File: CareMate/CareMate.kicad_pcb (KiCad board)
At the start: 2 copper layers, 19 parts, among them J1 Barrel_Jack_MountingPin, J2 Conn_01x16, J3 Conn_01x03, J4 Conn_01x03, J5 Conn_01x06, J6 Conn_01x03, J7 Conn_01x03, J8 Conn_01x02, U1 L7805, U2 LM386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

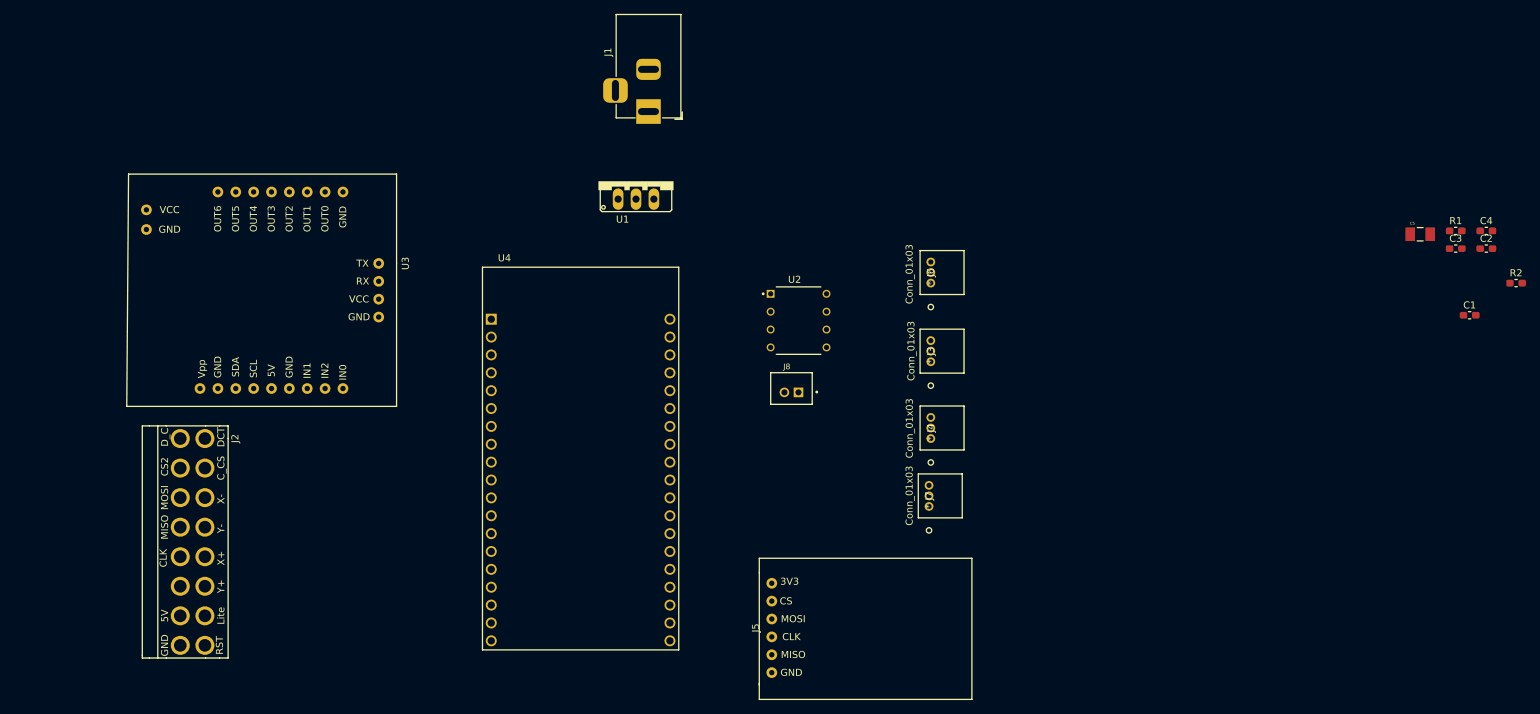
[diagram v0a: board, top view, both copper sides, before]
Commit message: significant PCB modifications including changes to elechouse footprint
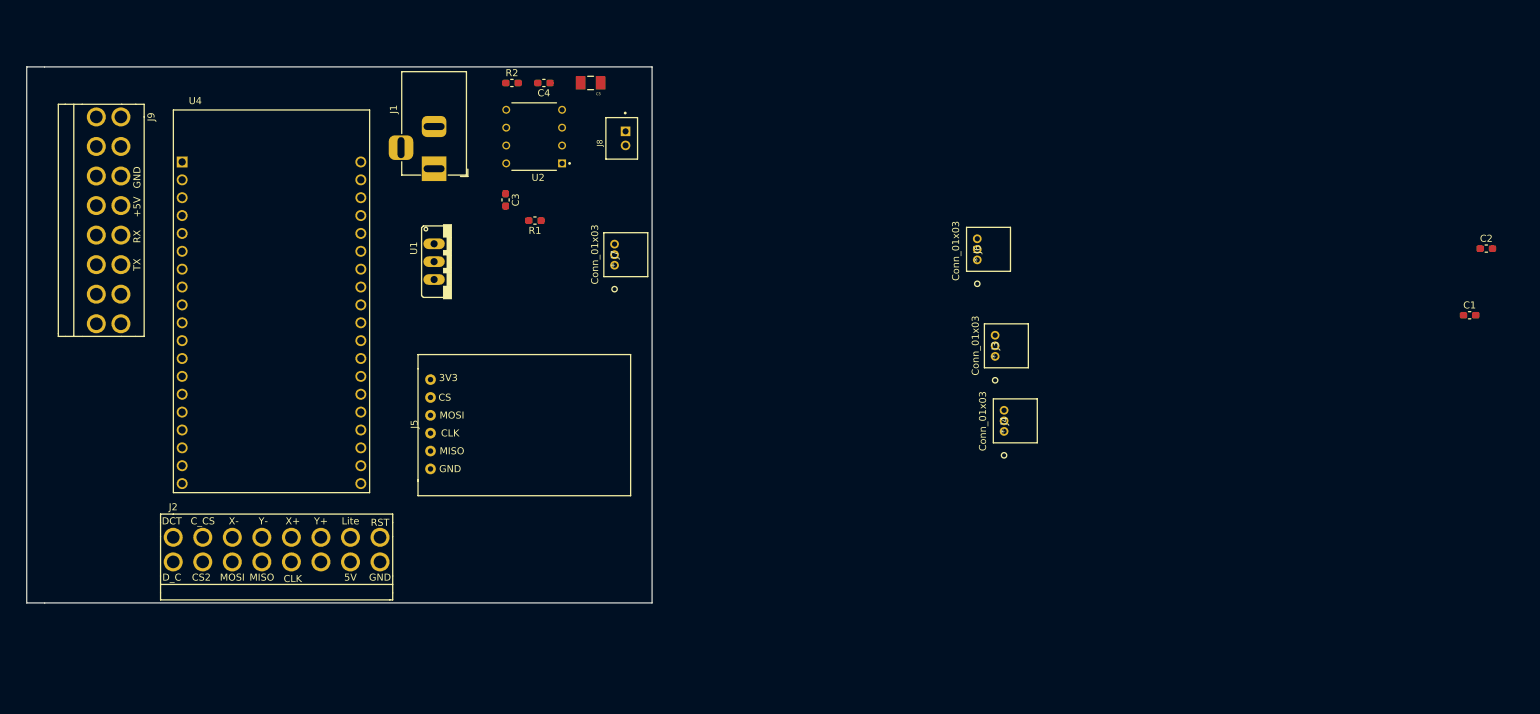
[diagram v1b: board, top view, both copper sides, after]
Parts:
- removed U3: Elechouse_V3, Additional Libraries:ElechouseV3
- added J9: ElechouseV3, Additional Libraries:16PinConnector, F.Cu at (63.8, 32.5)
- J2: value Conn_01x16 -> Touchscreen
- moved R2 145.6 mm to (117.2, 27.7)
- moved C4 135.6 mm to (121.8, 27.7), turned to 180 degrees
- moved C3 135.2 mm to (116.3, 44.3), turned to 270 degrees
- moved R1 130.9 mm to (120.5, 47.2), turned to 180 degrees
- moved C5 119.9 mm to (128.4, 27.7), turned to 180 degrees
- moved J5 56.5 mm to (105.7, 76.2)
- moved J7 56.3 mm to (131.8, 53.6)
- moved U4 49.3 mm to (83.1, 58.7)
- moved U2 45.8 mm to (120.4, 35.3), turned to 180 degrees
- moved J8 43.0 mm to (132.8, 35.6), turned to 90 degrees
- moved J1 31.5 mm to (106.2, 39.9)
- moved U1 28.5 mm to (108.7, 53.1), turned to 270 degrees
- moved J2 13.6 mm to (69.1, 90.2), turned to 0 degrees
- moved J4 10.5 mm to (187.2, 77.2)
- moved J3 9.18 mm to (185.9, 66.5)
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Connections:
- U1 pad 1: (no net) -> +9V
- U1 pad 2: (no net) -> GND
- U1 pad 3: (no net) -> +5V
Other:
- board outline added: 88.9 x 76.2 mm

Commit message: began running traces
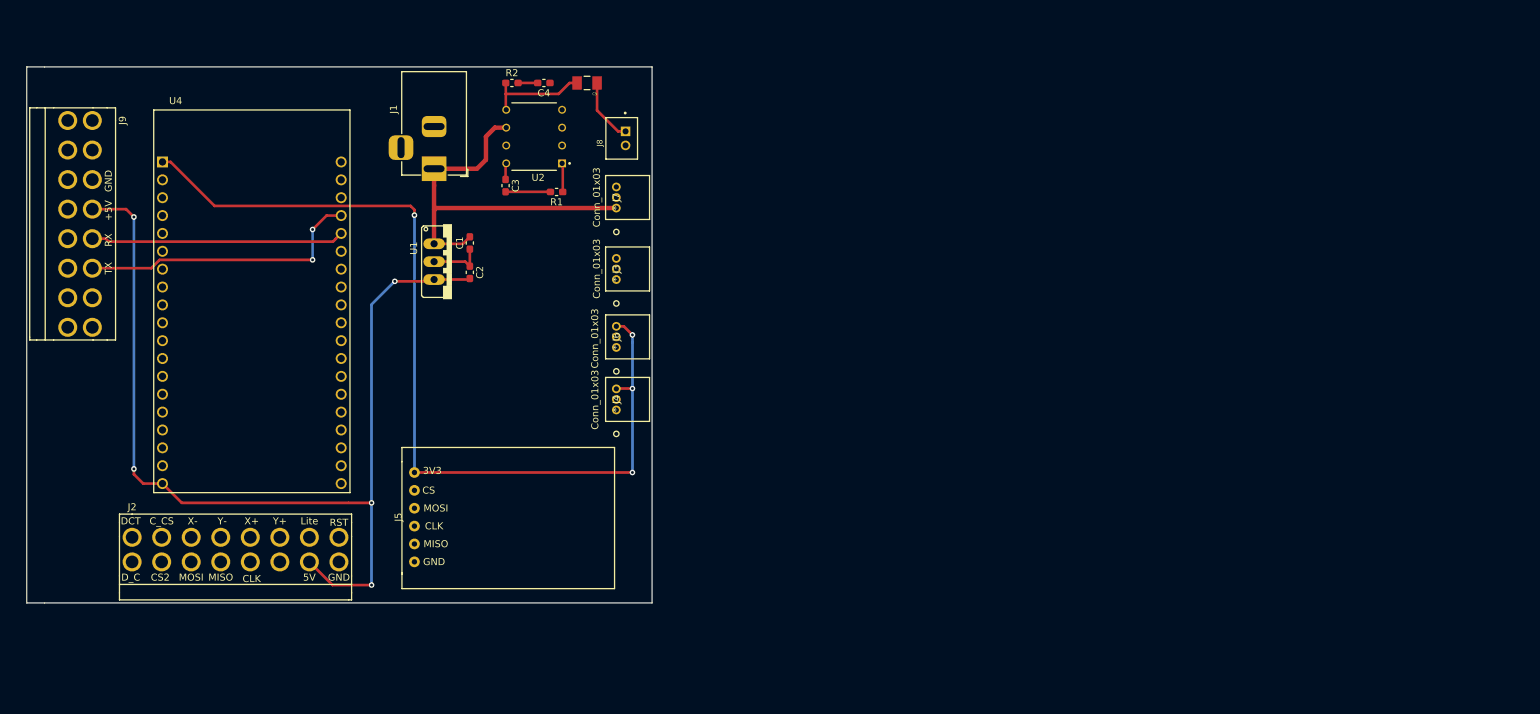
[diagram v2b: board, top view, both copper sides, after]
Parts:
- moved C2 144.5 mm to (111.3, 54.6), turned to 270 degrees
- moved C1 142.5 mm to (111.3, 50.4), turned to 90 degrees
- moved J4 55.2 mm to (132.1, 74.2)
- moved J3 54.9 mm to (132.1, 55.6)
- moved J6 52.8 mm to (132.1, 65.3)
- moved J5 13.4 mm to (103.4, 89.4)
- moved J7 8.13 mm to (132.1, 45.5)
- moved J2 5.84 mm to (63.2, 90.2)
- moved R1 5.10 mm to (123.6, 43.2)
- moved J9 4.10 mm to (59.7, 33.0)
- moved U4 2.79 mm to (80.3, 58.7)
- moved C3 2.03 mm to (116.3, 42.3)
- moved C5 0.51 mm to (127.9, 27.7)
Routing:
- net +5V: track 0.00 -> 144.0 mm, vias 0 -> 5
- net 3.3V: track 0.00 -> 131.6 mm, vias 0 -> 4
- net +9V: track 0.00 -> 56.8 mm
- net Tx_VoiceRec: track 0.00 -> 41.0 mm, vias 0 -> 2
- net Rx_VoiceRec: track 0.00 -> 36.0 mm
- net Net-(C5-Pad2): track 0.00 -> 14.6 mm
- net Amp_Output: track 0.00 -> 9.18 mm
- net GND: track 0.00 -> 7.78 mm
- net Net-(C3-Pad2): track 0.00 -> 6.39 mm
- net Net-(R1-Pad1): track 0.00 -> 4.10 mm
- net Net-(C4-Pad2): track 0.00 -> 2.79 mm
- net Net-(C3-Pad1): track 0.00 -> 2.32 mm

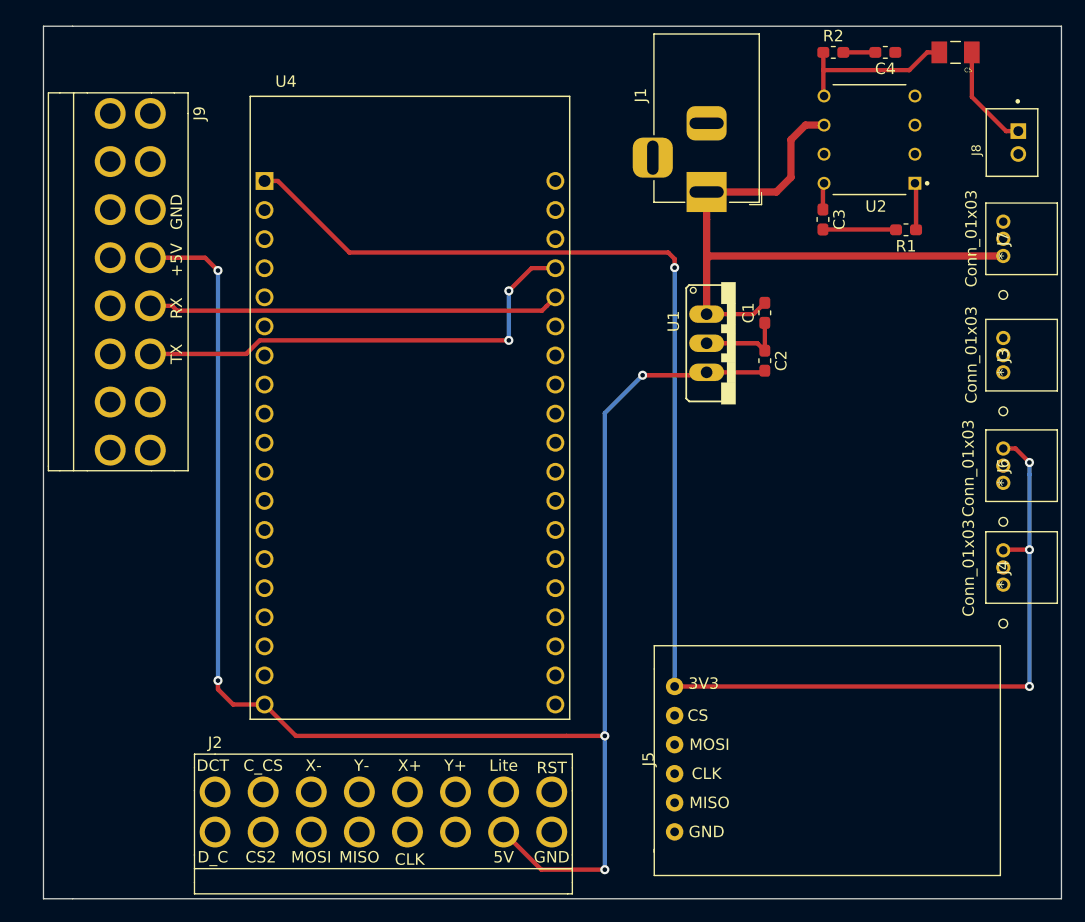
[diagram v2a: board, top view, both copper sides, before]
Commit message: Finished routing traces
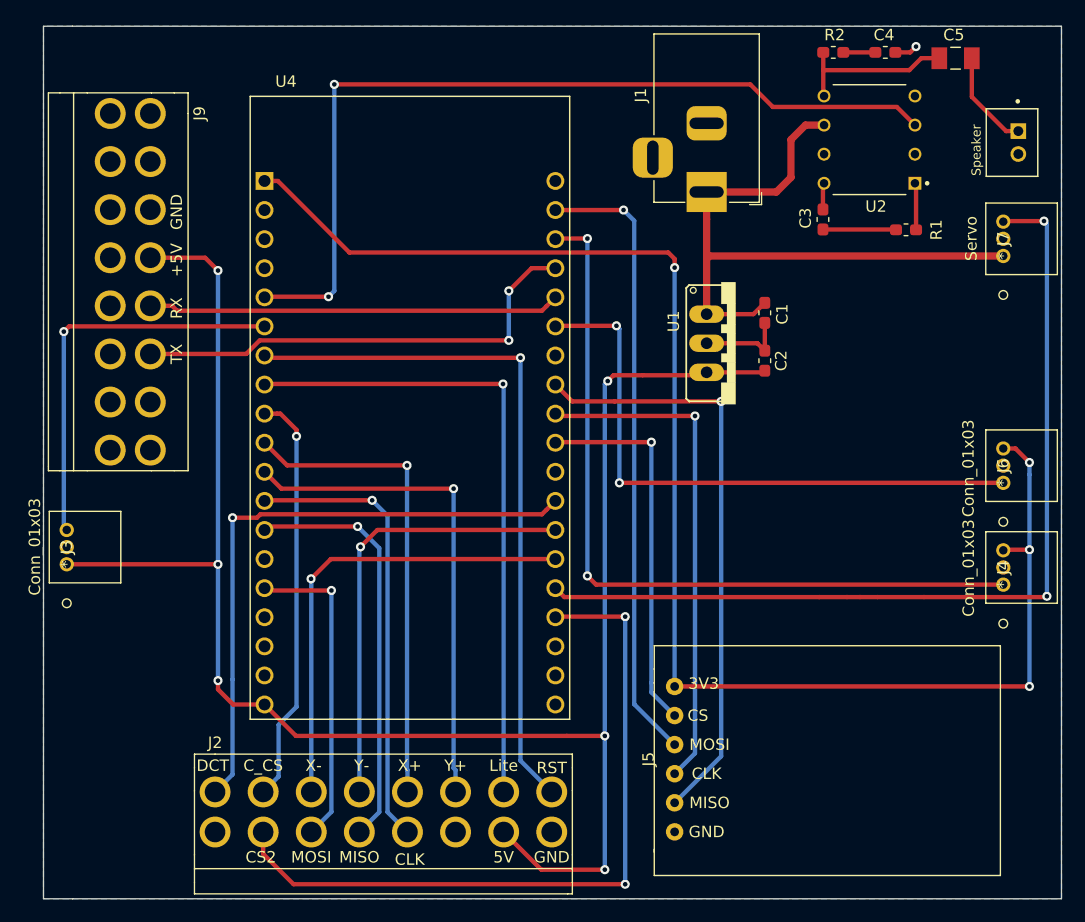
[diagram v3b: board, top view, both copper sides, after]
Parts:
- J2: value Touchscreen -> Conn_01x16
- J7: value Conn_01x03 -> Servo
- J9: value ElechouseV3 -> Conn_01x16
- moved J3 83.5 mm to (50.3, 72.4)
- moved C5 0.51 mm to (127.9, 28.2)
- renumbered J8 to Speaker
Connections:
- J2 pad 8: D_C -> Net-(J2-Pad8)
- U4 pad 6: D_C -> Mic_Out
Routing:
- net Servo_1: track 0.00 -> 79.7 mm, vias 0 -> 2
- net Unamplified_Signal: track 0.00 -> 76.5 mm, vias 0 -> 2
- net LS_1: track 0.00 -> 68.9 mm, vias 0 -> 2
- net CS2: track 0.00 -> 64.1 mm, vias 0 -> 2
- net RST: track 0.00 -> 61.5 mm, vias 0 -> 1
- net Lite: track 0.00 -> 56.5 mm, vias 0 -> 1
- net MOSI1: track 0.00 -> 54.5 mm, vias 0 -> 1
- net Card_Detect: track 0.00 -> 53.4 mm, vias 0 -> 1
- net LS_2: track 0.00 -> 52.7 mm, vias 0 -> 2
- net MISO1: track 0.00 -> 51.8 mm, vias 0 -> 1
- net clk1: track 0.00 -> 44.3 mm, vias 0 -> 1
- net Y+: track 0.00 -> 43.7 mm, vias 0 -> 1
- net X+: track 0.00 -> 41.8 mm, vias 0 -> 1
- net X-: track 0.00 -> 40.7 mm, vias 0 -> 1
- net clk2: track 0.00 -> 39.7 mm, vias 0 -> 1
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- added copper zone on B.Cu, net GND
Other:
- board text added: "CAREMATE REV 1 Senior Design 2"

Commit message: curved edgecuts
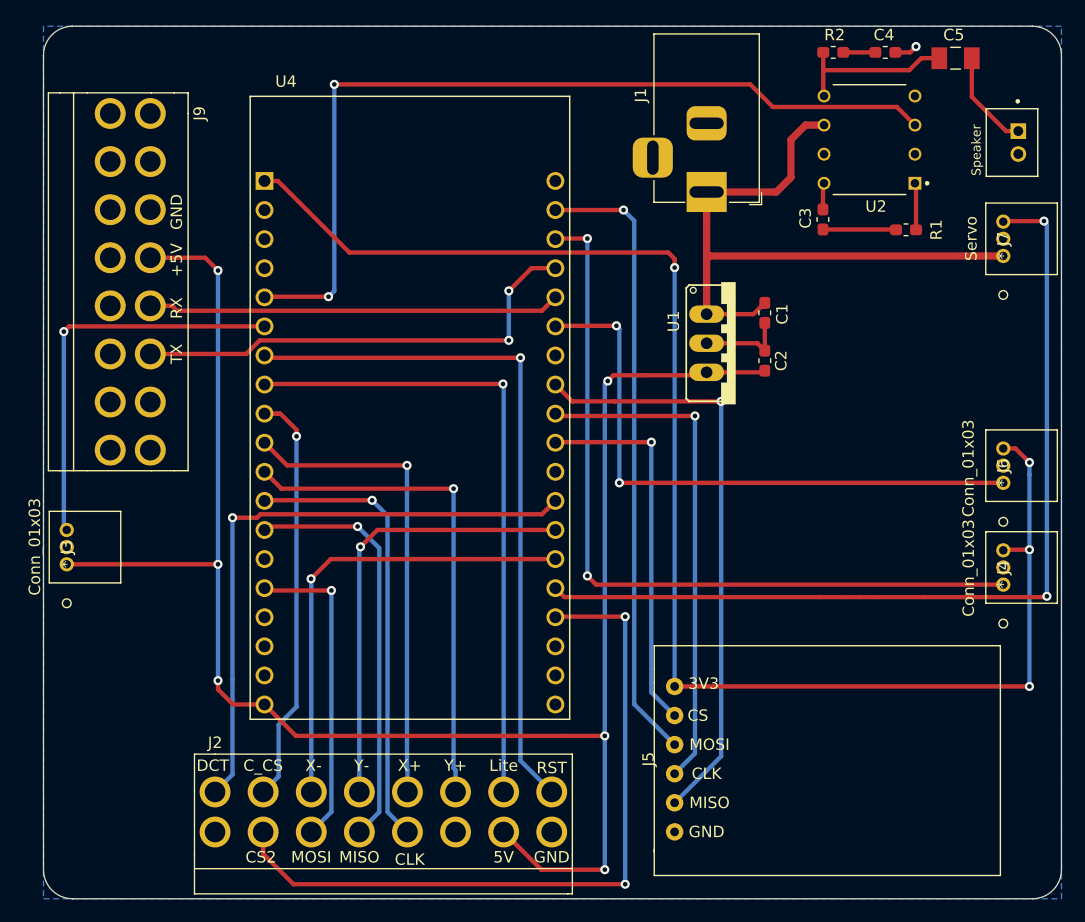
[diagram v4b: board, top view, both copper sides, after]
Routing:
- added copper zone on B.Cu, net (none)
- removed copper zone on B.Cu, net GND
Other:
- outline, holes or cut-outs redrawn
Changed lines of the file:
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@@
   (general
     (thickness 1.6)
-    (drawings 7)
+    (drawings 10)
     (tracks 240)
     (zones 0)
@@
       (net 61 "Net-(J9-Pad16)"))
   )
+  (gr_arc (start 134.62 27.94) (end 137.16 27.94) (angle -90) (layer Edge.Cuts) (width 0.05))
+  (gr_arc (start 50.8 27.94) (end 50.8 25.4) (angle -90) (layer Edge.Cuts) (width 0.05))
+  (gr_arc (start 50.8 99.06) (end 48.26 99.06) (angle -90) (layer Edge.Cuts) (width 0.05))
+  (gr_arc (start 134.62 99.06) (end 134.62 101.6) (angle -90) (layer Edge.Cuts) (width 0.05))
   (gr_text "CAREMATE REV 1\nSenior Design 2\n" (at 127.762 88.9) (layer B.SilkS)
     (effects (font (size 1 1) (thickness 0.15)) (justify mirror))
   )
-  (gr_line (start 48.26 25.4) (end 50.8 25.4) (layer Edge.Cuts) (width 0.05))
-  (gr_line (start 50.8 101.6) (end 48.26 101.6) (layer Edge.Cuts) (width 0.05))
-  (gr_line (start 48.26 25.4) (end 48.26 101.6) (layer Edge.Cuts) (width 0.05))
-  (gr_line (start 137.16 25.4) (end 50.8 25.4) (layer Edge.Cuts) (width 0.05))
-  (gr_line (start 137.16 101.6) (end 137.16 25.4) (layer Edge.Cuts) (width 0.05))
-  (gr_line (start 50.8 101.6) (end 137.16 101.6) (layer Edge.Cuts) (width 0.05))
+  (gr_line (start 50.8 25.4) (end 50.8 25.4) (layer Edge.Cuts) (width 0.05))
+  (gr_line (start 48.26 27.94) (end 48.26 99.06) (layer Edge.Cuts) (width 0.05))
+  (gr_line (start 134.62 25.4) (end 50.8 25.4) (layer Edge.Cuts) (width 0.05))
+  (gr_line (start 137.16 99.06) (end 137.16 27.94) (layer Edge.Cuts) (width 0.05))
+  (gr_line (start 50.8 101.6) (end 134.62 101.6) (layer Edge.Cuts) (width 0.05))
   (segment (start 106.172 39.878) (end 106.172 42.263) (width 0.635) (layer F.Cu) (net 1))
   (segment (start 112.268 39.878) (end 106.172 39.878) (width 0.635) (layer F.Cu) (net 1))
@@
   (segment (start 59.499188 49.82) (end 59.923689 50.244501) (width 0.381) (layer F.Cu) (net 37))
   (segment (start 57.59 49.82) (end 59.499188 49.82) (width 0.381) (layer F.Cu) (net 37))
-  (zone (net 2) (net_name GND) (layer B.Cu) (hatch edge 0.508)
+  (zone (net 0) (net_name "") (layer B.Cu) (hatch edge 0.508)
     (connect_pads yes (clearance 0.508))
     (min_thickness 0.254)

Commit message: added silkscreens
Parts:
- added G***: LOGO, Additional Libraries:discgolf, F.Cu at (58.7, 69.8)
- added G***: LOGO, Additional Libraries:cheese, F.Cu at (129.3, 51.1)
- added G***: LOGO, Additional Libraries:carmex, F.Cu at (57.7, 80.3)
- added G***: LOGO, Additional Libraries:cyclone, F.Cu at (55.9, 93.2)
- added G***: LOGO, Additional Libraries:lifealertlady, F.Cu at (113.3, 60.2)
